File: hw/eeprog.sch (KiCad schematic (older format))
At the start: 7 parts, among them U1 74HC595, U2 74HC595, U3 74HC595, U4 28C256, U5 74HC165

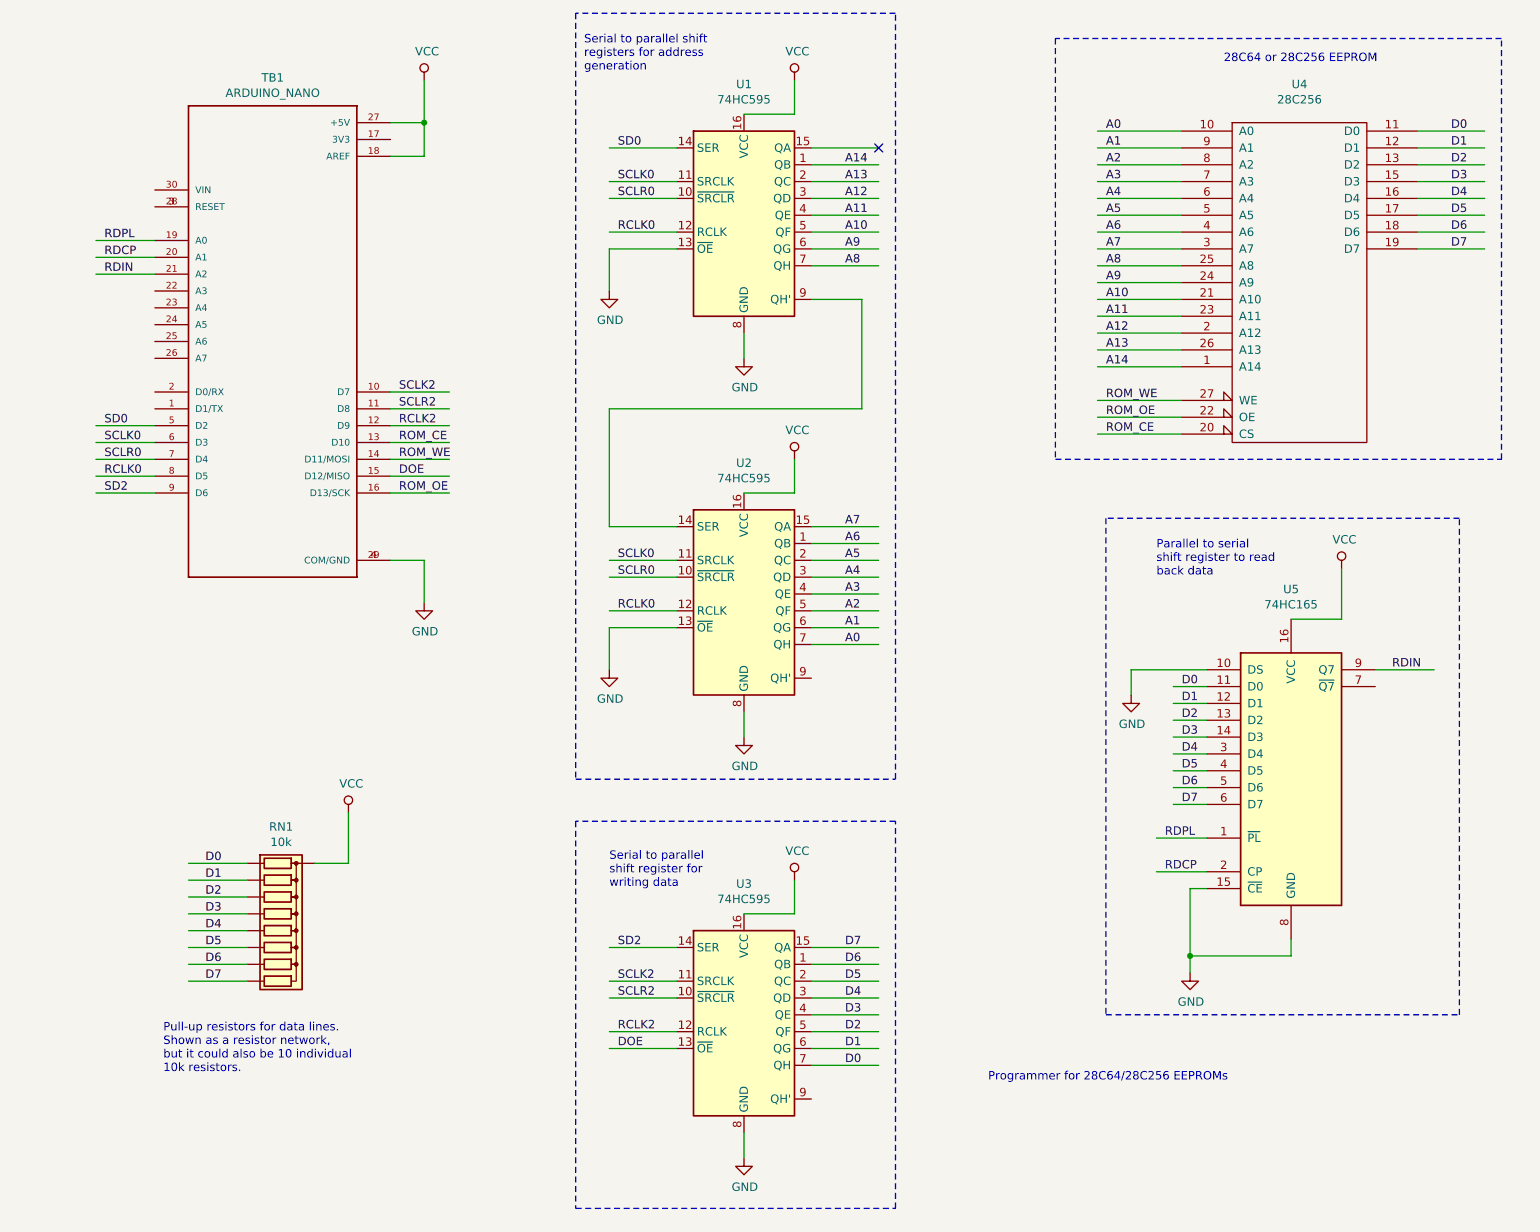
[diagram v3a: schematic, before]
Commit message: add indicator LEDs and decoupling caps
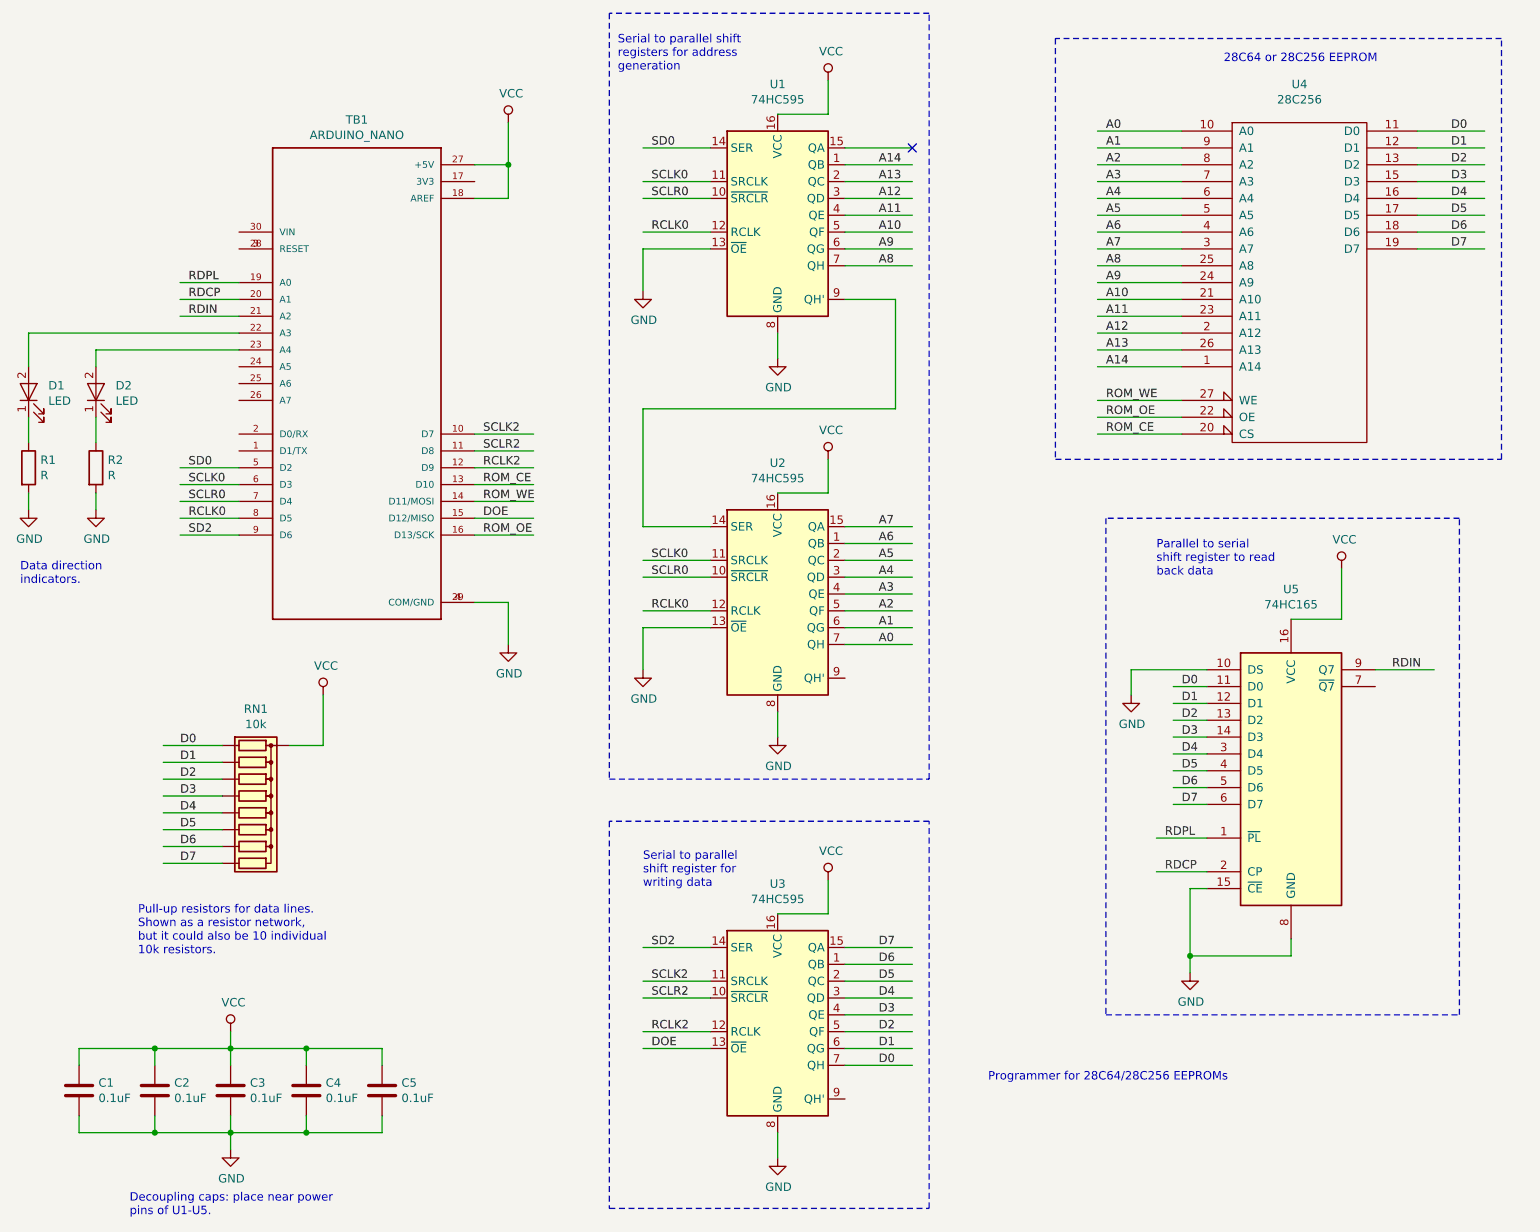
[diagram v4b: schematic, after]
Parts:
- added C1, C2, C3, C4, C5: 0.1uF, symbol device:C
- added D1, D2: LED, symbol device:LED
- added R1, R2: R, symbol device:R
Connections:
- wire segments 131 -> 159
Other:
- note added: "Data direction\nindicators."
- note added: "Decoupling caps: place near power\npins of U1-U5."
- moved on the sheet: RN1, TB1, U1, U2, U3

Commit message: add delays when pulsing '165 to latch read data
Was having some trouble reading back data from the
'165 shift register.  Added some delays when clocking
it.  We'll see if that fixes the problem.

Also, changed the '165 shift register device name
from 74HC165 to 74HCT165 in the schematic.  HCT
logic is a better choice, since I have observed
memory devices outputting TTL level signals, which
might not reliably drive the inputs of 74HC chips.
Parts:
- U5: value 74HC165 -> 74HCT165
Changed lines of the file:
@@
 P 8250 5100
 F 0 "U5" H 8250 6178 50  0000 C CNN
-F 1 "74HC165" H 8250 6087 50  0000 C CNN
+F 1 "74HCT165" H 8250 6087 50  0000 C CNN
 F 2 "" H 8250 5100 50  0001 C CNN
 F 3 "" H 8250 5100 50  0001 C CNN

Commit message: fix eeprom power
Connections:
- wire segments 159 -> 162
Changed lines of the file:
@@
 Wire Notes Line
 	4200 5400 4200 7700
-Text Notes 7850 900  0    50   ~ 0
+Text Notes 7550 800  0    50   ~ 0
 28C64 or 28C256 EEPROM
-Wire Notes Line
-	6850 750  6850 3250
-Wire Notes Line
-	6850 3250 9500 3250
-Wire Notes Line
-	9500 3250 9500 750
-Wire Notes Line
-	9500 750  6850 750
 Text Notes 7450 3950 0    50   ~ 0
 Parallel to serial\nshift register to read\nback data
@@
 Text Notes 700  4000 0    50   ~ 0
 Data direction\nindicators.
+$Comp
+L power:GND #PWR?
+U 1 1 5D81E85C
+P 8300 3150
+F 0 "#PWR?" H 8300 2900 50  0001 C CNN
+F 1 "GND" H 8305 2977 50  0000 C CNN
+F 2 "" H 8300 3150 50  0001 C CNN
+F 3 "" H 8300 3150 50  0001 C CNN
+	1    8300 3150
+	1    0    0    -1
+$EndComp
+Wire Notes Line
+	9650 600  9650 3400
+Wire Notes Line
+	6650 600  9650 600
+Wire Notes Line
+	6650 3400 9650 3400
+Wire Notes Line
+	6650 600  6650 3400
+Wire Wire Line
+	8500 1250 8500 1100
+Wire Wire Line
+	8500 1100 8900 1100
+Wire Wire Line
+	8900 1100 8900 1000
+$Comp
+L power:VCC #PWR?
+U 1 1 5D881F1E
+P 8900 1000
+F 0 "#PWR?" H 8900 850 50  0001 C CNN
+F 1 "VCC" H 8917 1173 50  0000 C CNN
+F 2 "" H 8900 1000 50  0001 C CNN
+F 3 "" H 8900 1000 50  0001 C CNN
+	1    8900 1000
+	1    0    0    -1
+$EndComp
 $EndSCHEMATC
